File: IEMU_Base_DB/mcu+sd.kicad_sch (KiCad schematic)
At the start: 27 parts, among them J301 Conn_ARM_SWD_TagConnect_TC203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, J302 503398-1892, U301 Ezurio BL54L15, U302 TMUX1204DQAR, Y201 32.768kHz

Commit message: implemented changes from the review with TF and fixed lost parts in the library
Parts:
- removed D301, D302, D303, D304, D305: RCLAMP3321P-N, Diode_SMD:D_SOD-882, symbol 0_Connectors:RCLAMP3321P-N
- added D301, D302, D303, D304, D305: ESD9L1P8, Diode_SMD:D_SOD-882, symbol 0_Power:ESD9L1P8
- FL301: Distributor Link 1 https://www.mouser.co.uk/ProductDetail/STMicroelectronics/E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 -> https://www.mouser.de/ProductDetail/STMicroelectronics/EMIF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; Distributor Link 2 https://www.digikey.com/en/products/detail/stmicroelectroni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 -> https://www.digikey.de/de/products/detail/stmicroelectronic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
- J302: Distributor Link 2 https://www.digikey.de/de/products/detail/molex/5033981892/4555393?s=N4IgTCBcDaIKwAYDMSCcAOAjO1EC6AvkA -> https://www.digikey.de/de/products/detail/molex/5033981892/4555393?s=N4IgTCBcDaIKwAYDMSCcAOAtARnaiAugL5A; Manufacturer_Name molex -> Molex; Manufacturer_Part_Number 503398-1892 -> 503398-1892
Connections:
- net +1V8_MCU: now also D305.1 (I/O)
- net GND: now also D301.2 (GND), D302.2 (GND), D303.2 (GND), D304.2 (GND), D305.2 (GND)
- net SWD_CLK: now also D301.1 (I/O)
- net SWD_IO: now also D302.1 (I/O)
- net SWD_O: now also D303.1 (I/O)
- net SWD_RESET: now also D304.1 (I/O)

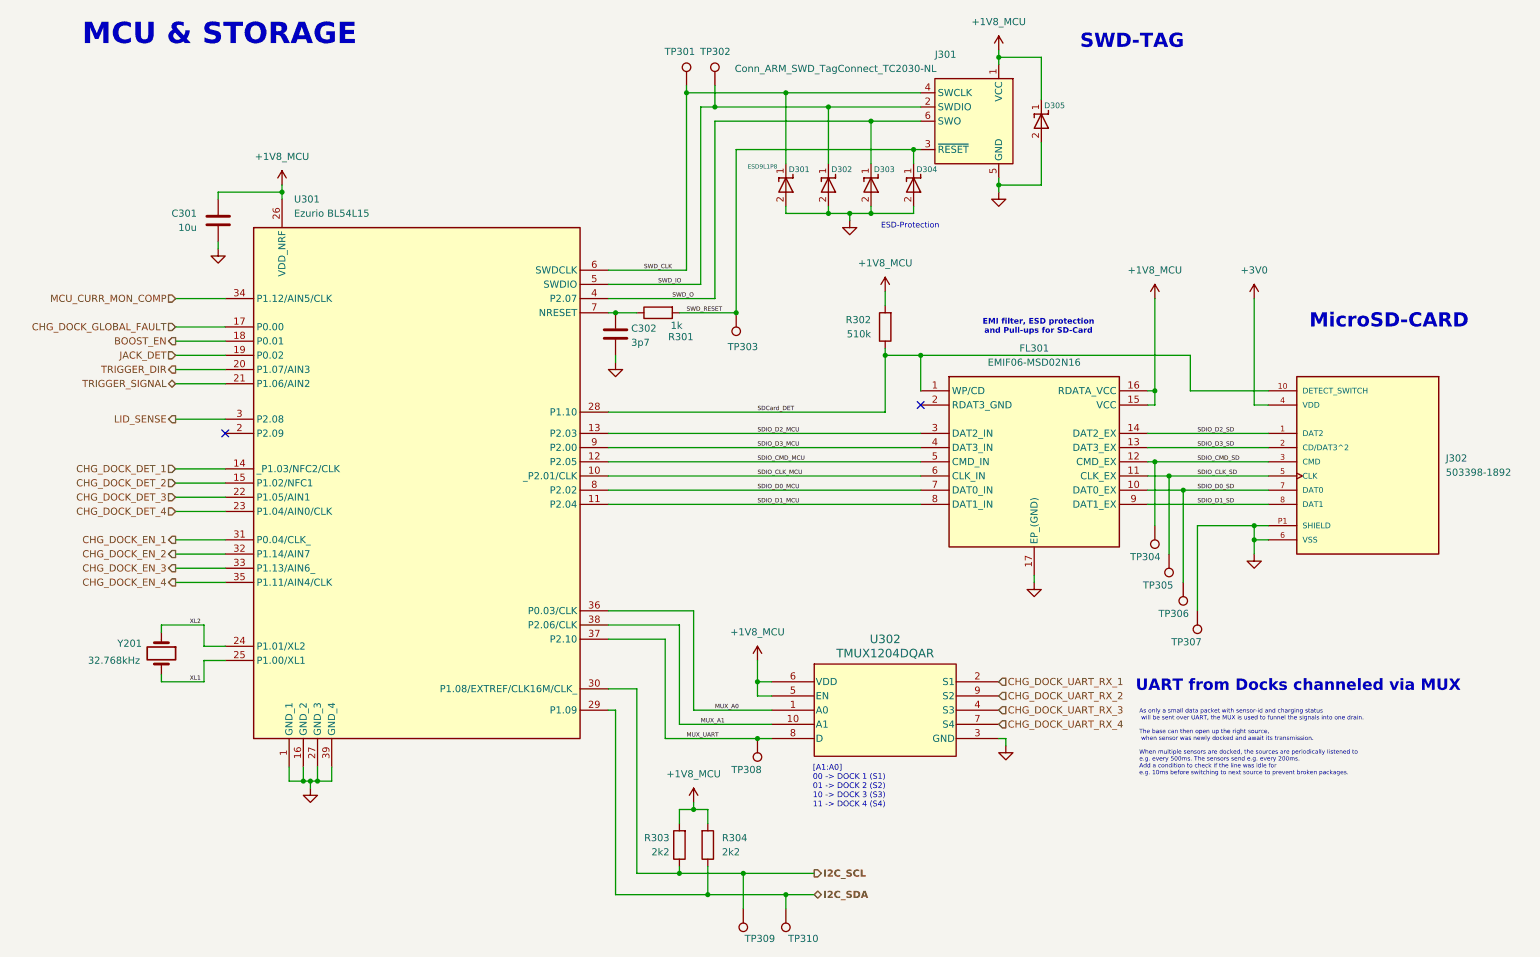
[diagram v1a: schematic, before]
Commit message: layout of base and some fixes on the sensor layout
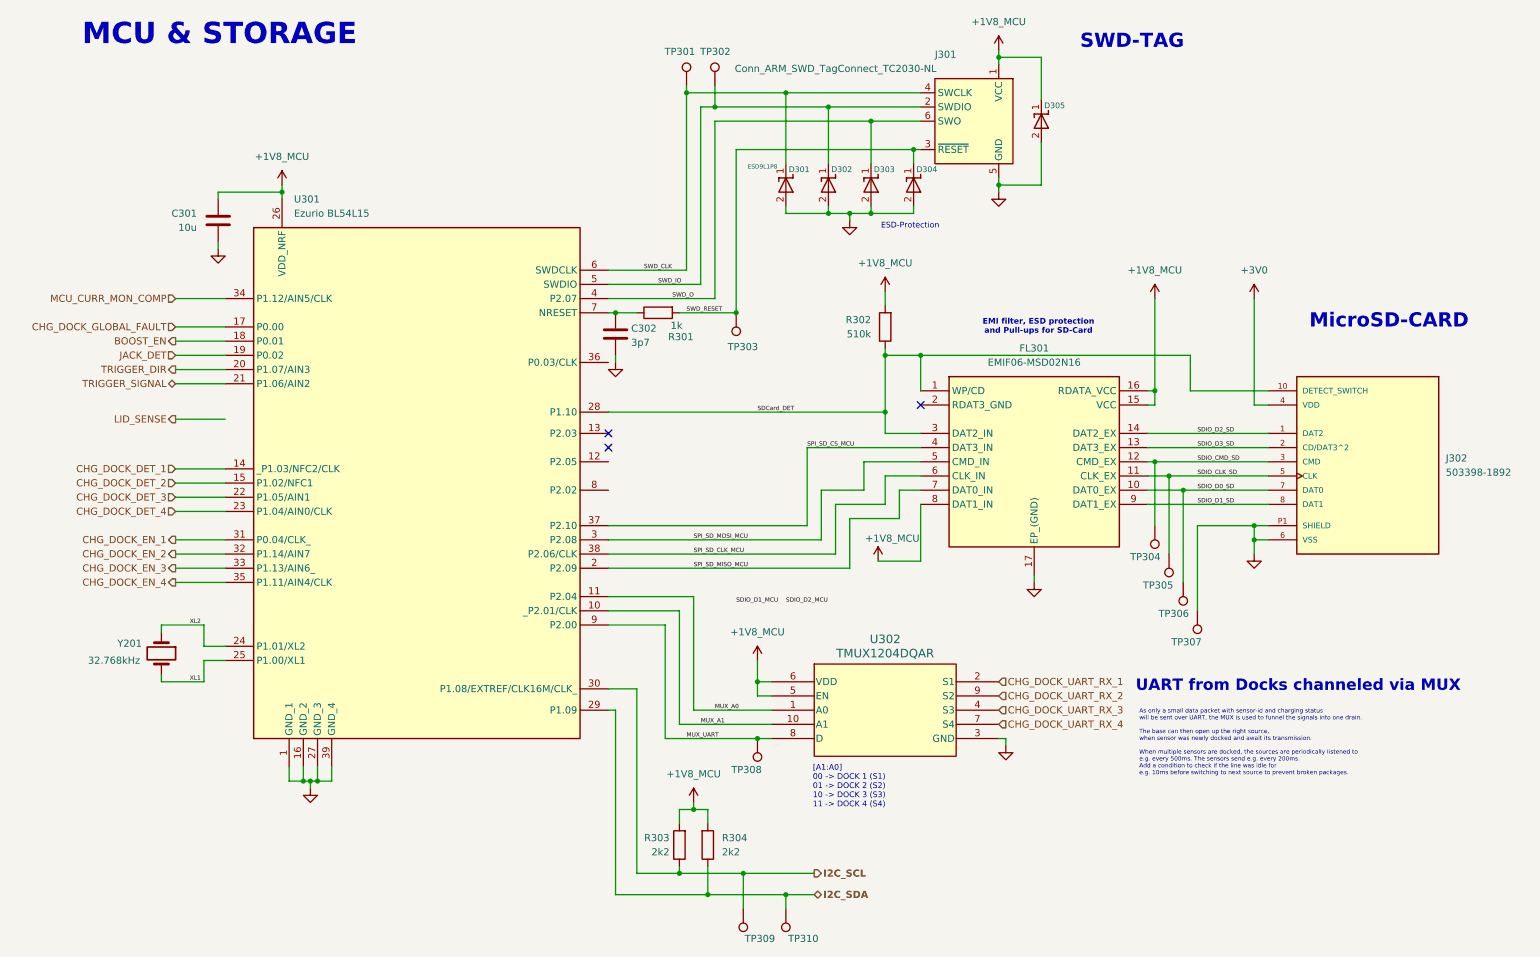
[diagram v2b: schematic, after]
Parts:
- TP301, TP302, TP303, TP309, TP310: footprint TestPoint:TestPoint_Pad_D2.0mm -> TestPoint:TestPoint_Pad_D1.0mm
- TP304, TP305, TP306, TP307, TP308: footprint TestPoint:TestPoint_Pad_D0.6mm -> TestPoint:TestPoint_Pad_D1.0mm
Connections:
- net +1V8_MCU: now also FL301.8 (DAT1_IN)
- net LID_SENSE: no longer U301.3 (P2.08)
- net MUX_A0: now also U301.11 (P2.04); no longer U301.36 (P0.03/CLK)
- net MUX_A1: now also U301.10 (_P2.01/CLK); no longer U301.38 (P2.06/CLK)
- net MUX_UART: now also U301.9 (P2.00); no longer U301.37 (P2.10)
- net SDCard_DET: now also FL301.3 (DAT2_IN)
- net SDIO_D1_MCU: no longer FL301.8 (DAT1_IN), U301.11 (P2.04)
- net SDIO_D2_MCU: no longer FL301.3 (DAT2_IN), U301.13 (P2.03)
- net SPI_SD_MISO_MCU: now reaches U301.2 (P2.09)
- net SPI_SD_MISO_MCU: now also FL301.7 (DAT0_IN)
- net SDIO_CLK_MCU renamed SPI_SD_CLK_MCU
- net SPI_SD_CLK_MCU: now also U301.38 (P2.06/CLK); no longer U301.10 (_P2.01/CLK)
- net SDIO_CMD_MCU: no longer names the net of U301.12 (P2.05)
- net SDIO_CMD_MCU: no longer FL301.5 (CMD_IN)
- net SDIO_D0_MCU: no longer names the net of U301.8 (P2.02)
- net SDIO_D0_MCU: no longer FL301.7 (DAT0_IN)
- net SDIO_D3_MCU renamed SPI_SD_CS_MCU
- net SPI_SD_CS_MCU: now also U301.37 (P2.10); no longer U301.9 (P2.00)
- new net SPI_SD_MOSI_MCU: FL301.5 (CMD_IN), U301.3 (P2.08)
- no-connect marks 2 -> 3
